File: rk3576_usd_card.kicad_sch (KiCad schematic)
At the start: 2 parts, among them U27 RK3576

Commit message: Add files via upload
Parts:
- renumbered C265 to C143, U27 to U2
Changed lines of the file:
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@@
 		(dnp no)
 		(fields_autoplaced yes)
-		(property "Reference" "C265"
+		(property "Reference" "C143"
 			(at 58.42 71.1262 0)
 			(show_name no)
@@
 		)
 		(property "Description" "Unpolarized capacitor, small symbol"
+			(at 60.96 72.39 0)
+			(hide yes)
+			(show_name no)
+			(do_not_autoplace no)
+			(effects
+				(font
+					(size 1.27 1.27)
+				)
+			)
+		)
+		(property "Dielectric" ""
+			(at 60.96 72.39 0)
+			(hide yes)
+			(show_name no)
+			(do_not_autoplace no)
+			(effects
+				(font
+					(size 1.27 1.27)
+				)
+			)
+		)
+		(property "Voltage" ""
+			(at 60.96 72.39 0)
+			(hide yes)
+			(show_name no)
+			(do_not_autoplace no)
+			(effects
+				(font
+					(size 1.27 1.27)
+				)
+			)
+		)
+		(property "KLC_S3.3" ""
+			(at 60.96 72.39 0)
+			(hide yes)
+			(show_name no)
+			(do_not_autoplace no)
+			(effects
+				(font
+					(size 1.27 1.27)
+				)
+			)
+		)
+		(property "KLC_S4.1" ""
+			(at 60.96 72.39 0)
+			(hide yes)
+			(show_name no)
+			(do_not_autoplace no)
+			(effects
+				(font
+					(size 1.27 1.27)
+				)
+			)
+		)
+		(property "KLC_S5.1" ""
 			(at 60.96 72.39 0)
 			(hide yes)
@@
 			(project "RK3576 SBC"
 				(path "/b79dbff4-0cad-4ff7-bec2-7c0e4f8b14d3/34f9b0cb-aeae-42b4-a2af-a0a79afcf392/e3169b31-7633-42aa-8b59-c93f8fc73ecf"
-					(reference "C265")
+					(reference "C143")
 					(unit 1)
 				)
@@
 		(in_pos_files yes)
 		(dnp no)
-		(property "Reference" "#PWR0352"
+		(property "Reference" "#PWR0205"
 			(at 60.96 81.28 0)
 			(hide yes)
@@
 			(project "RK3576 SBC"
 				(path "/b79dbff4-0cad-4ff7-bec2-7c0e4f8b14d3/34f9b0cb-aeae-42b4-a2af-a0a79afcf392/e3169b31-7633-42aa-8b59-c93f8fc73ecf"
-					(reference "#PWR0352")
+					(reference "#PWR0205")
 					(unit 1)
 				)
@@
 		(in_pos_files yes)
 		(dnp no)
-		(property "Reference" "#PWR0351"
+		(property "Reference" "#PWR0204"
 			(at 60.96 68.58 0)
 			(hide yes)
@@
 			(project "RK3576 SBC"
 				(path "/b79dbff4-0cad-4ff7-bec2-7c0e4f8b14d3/34f9b0cb-aeae-42b4-a2af-a0a79afcf392/e3169b31-7633-42aa-8b59-c93f8fc73ecf"
-					(reference "#PWR0351")
+					(reference "#PWR0204")
 					(unit 1)
 				)
@@
 		(dnp no)
 		(fields_autoplaced yes)
-		(property "Reference" "U27"
+		(property "Reference" "U2"
 			(at 101.6 62.23 0)
 			(show_name no)
@@
 		(property "Package" "FCCSP698L"
 			(at 101.6 72.39 0)
+			(show_name no)
+			(do_not_autoplace no)
+			(effects
+				(font
+					(size 1.27 1.27)
+				)
+			)
+		)
+		(property "Dielectric" ""
+			(at 101.6 87.63 0)
+			(hide yes)
+			(show_name no)
+			(do_not_autoplace no)
+			(effects
+				(font
+					(size 1.27 1.27)
+				)
+			)
+		)
+		(property "Voltage" ""
+			(at 101.6 87.63 0)
+			(hide yes)
+			(show_name no)
+			(do_not_autoplace no)
+			(effects
+				(font
+					(size 1.27 1.27)
+				)
+			)
+		)
+		(property "KLC_S3.3" ""
+			(at 101.6 87.63 0)
+			(hide yes)
+			(show_name no)
+			(do_not_autoplace no)
+			(effects
+				(font
+					(size 1.27 1.27)
+				)
+			)
+		)
+		(property "KLC_S4.1" ""
+			(at 101.6 87.63 0)
+			(hide yes)
+			(show_name no)
+			(do_not_autoplace no)
+			(effects
+				(font
+					(size 1.27 1.27)
+				)
+			)
+		)
+		(property "KLC_S5.1" ""
+			(at 101.6 87.63 0)
+			(hide yes)
 			(show_name no)
 			(do_not_autoplace no)
@@
 			(project "RK3576 SBC"
 				(path "/b79dbff4-0cad-4ff7-bec2-7c0e4f8b14d3/34f9b0cb-aeae-42b4-a2af-a0a79afcf392/e3169b31-7633-42aa-8b59-c93f8fc73ecf"
-					(reference "U27")
+					(reference "U2")
 					(unit 16)
 				)

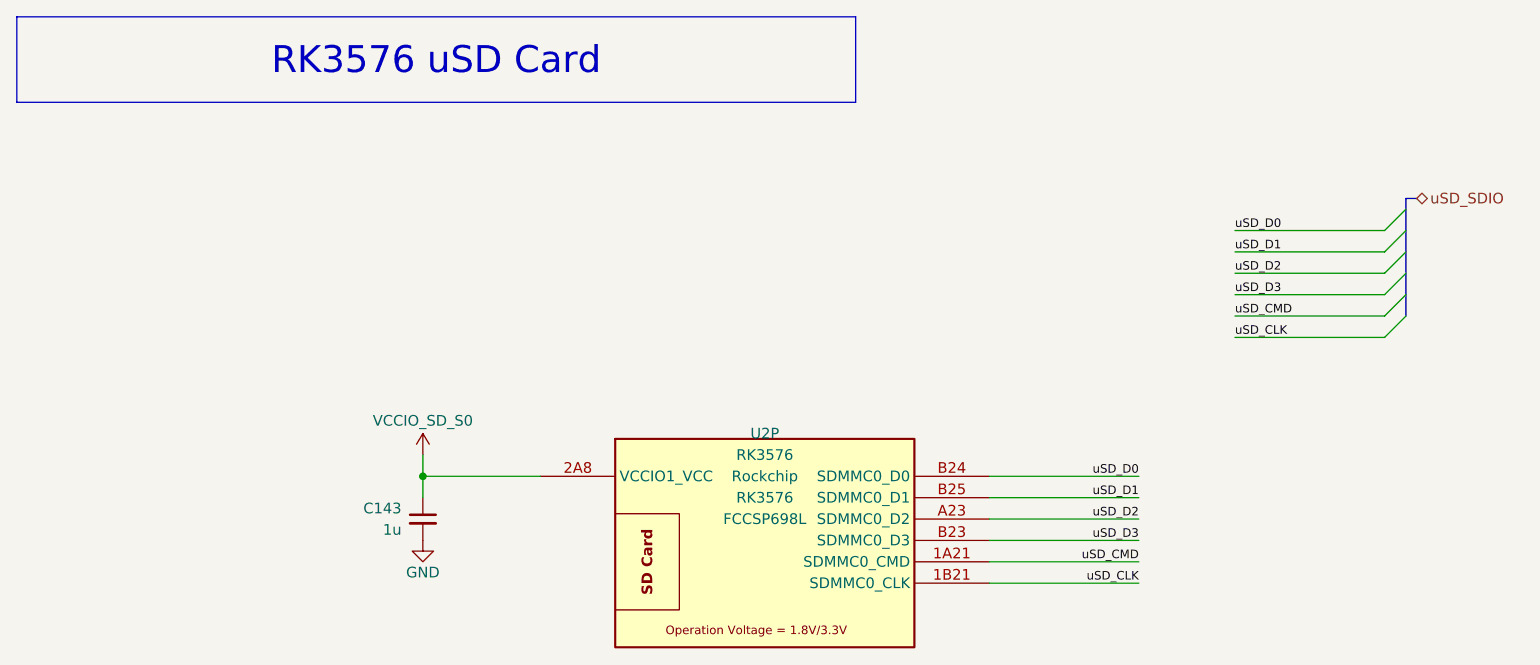
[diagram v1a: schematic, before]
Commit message: SBC Board V0.2
The SBC schematics before footprint and part number check
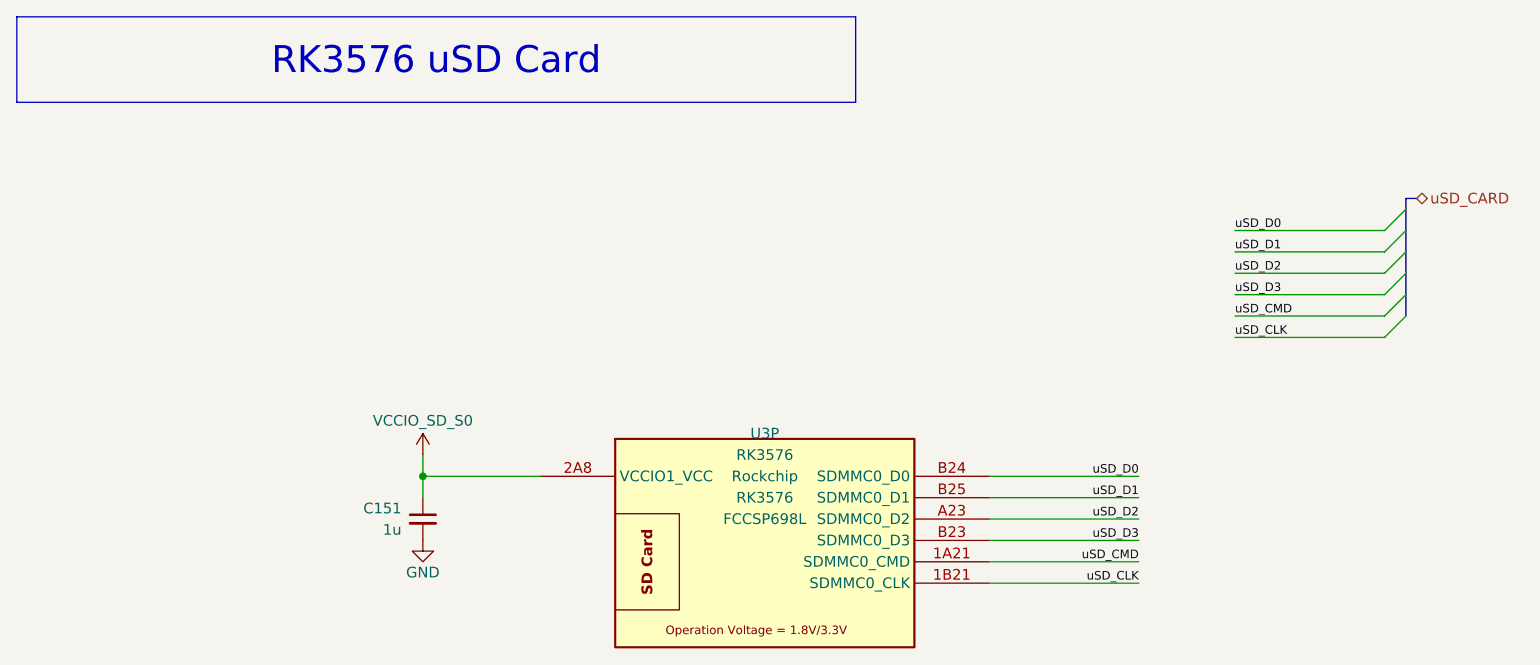
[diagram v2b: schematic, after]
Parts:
- U3: renamed from U2; footprint (none) -> easyeda2kicad:FCCSP-698_L17.2-W16.1-TL_RK3576
- renumbered C143 to C151
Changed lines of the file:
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@@
 		)
 	)
-	(hierarchical_label "uSD_SDIO"
+	(hierarchical_label "uSD_CARD"
 		(shape bidirectional)
 		(at 179.07 34.29 0)
+		(fields_autoplaced yes)
 		(effects
 			(font
@@
 			)
 			(justify left)
+		)
+		(property "Netclass" "uSD_CARD"
+			(at 179.07 35.56 0)
+			(hide yes)
+			(show_name no)
+			(do_not_autoplace no)
+			(effects
+				(font
+					(size 1.27 1.27)
+					(italic yes)
+				)
+				(justify left)
+			)
 		)
 	)
@@
 		(dnp no)
 		(fields_autoplaced yes)
-		(property "Reference" "C143"
+		(property "Reference" "C151"
 			(at 58.42 71.1262 0)
 			(show_name no)
@@
 			(project "RK3576 SBC"
 				(path "/b79dbff4-0cad-4ff7-bec2-7c0e4f8b14d3/34f9b0cb-aeae-42b4-a2af-a0a79afcf392/e3169b31-7633-42aa-8b59-c93f8fc73ecf"
-					(reference "C143")
+					(reference "C151")
 					(unit 1)
 				)
@@
 		(in_pos_files yes)
 		(dnp no)
-		(property "Reference" "#PWR0205"
+		(property "Reference" "#PWR0217"
 			(at 60.96 81.28 0)
 			(hide yes)
@@
 			(project "RK3576 SBC"
 				(path "/b79dbff4-0cad-4ff7-bec2-7c0e4f8b14d3/34f9b0cb-aeae-42b4-a2af-a0a79afcf392/e3169b31-7633-42aa-8b59-c93f8fc73ecf"
-					(reference "#PWR0205")
+					(reference "#PWR0217")
 					(unit 1)
 				)
@@
 		(in_pos_files yes)
 		(dnp no)
-		(property "Reference" "#PWR0204"
+		(property "Reference" "#PWR0216"
 			(at 60.96 68.58 0)
 			(hide yes)
@@
 			(project "RK3576 SBC"
 				(path "/b79dbff4-0cad-4ff7-bec2-7c0e4f8b14d3/34f9b0cb-aeae-42b4-a2af-a0a79afcf392/e3169b31-7633-42aa-8b59-c93f8fc73ecf"
-					(reference "#PWR0204")
+					(reference "#PWR0216")
 					(unit 1)
 				)
@@
 		(dnp no)
 		(fields_autoplaced yes)
-		(property "Reference" "U2"
+		(property "Reference" "U3"
 			(at 101.6 62.23 0)
 			(show_name no)
@@
 			)
 		)
-		(property "Footprint" ""
+		(property "Footprint" "easyeda2kicad:FCCSP-698_L17.2-W16.1-TL_RK3576"
 			(at 34.29 24.765 0)
 			(hide yes)
@@
 			(project "RK3576 SBC"
 				(path "/b79dbff4-0cad-4ff7-bec2-7c0e4f8b14d3/34f9b0cb-aeae-42b4-a2af-a0a79afcf392/e3169b31-7633-42aa-8b59-c93f8fc73ecf"
-					(reference "U2")
+					(reference "U3")
 					(unit 16)
 				)

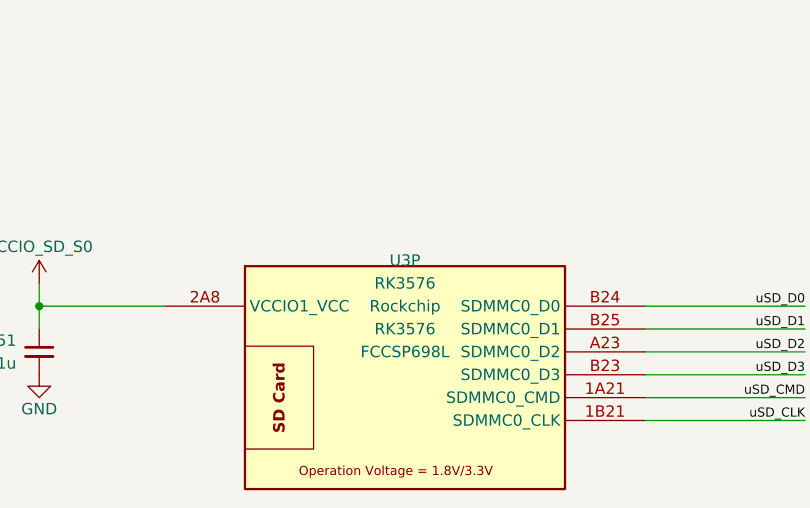
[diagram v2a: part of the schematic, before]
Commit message: SBCv0.3
there is no big thing update just some LCSC & Mouser parts
and Big problem deleted alot of component values (:
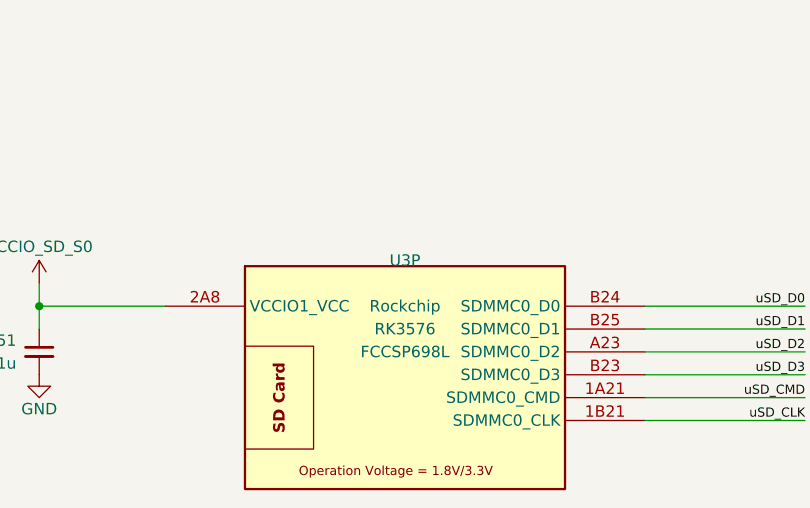
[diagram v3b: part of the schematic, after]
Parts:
- C151: footprint Capacitor_SMD:C_0402_1005Metric_Pad0.74x0.62mm_HandSolder -> Capacitor_SMD:C_0201_0603Metric_Pad0.64x0.40mm_HandSolder; LCSC Part (none) -> C5209398; Mouser Part (none) -> CL03A105KP3NSNC
- U3: value RK3576 -> (none); LCSC Part (none) -> (polyline
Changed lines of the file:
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@@
 			)
 		)
-		(property "Footprint" "Capacitor_SMD:C_0402_1005Metric_Pad0.74x0.62mm_HandSolder"
+		(property "Footprint" "Capacitor_SMD:C_0201_0603Metric_Pad0.64x0.40mm_HandSolder"
 			(at 60.96 72.39 0)
 			(hide yes)
@@
 			)
 		)
-		(property "KLC_S5.1" ""
+		(property "LCSC Part" "C5209398"
+			(at 60.96 72.39 0)
+			(hide yes)
+			(show_name no)
+			(do_not_autoplace no)
+			(effects
+				(font
+					(size 1.27 1.27)
+				)
+			)
+		)
+		(property "Mouser Part" "CL03A105KP3NSNC "
+			(at 60.96 72.39 0)
+			(hide yes)
+			(show_name no)
+			(do_not_autoplace no)
+			(effects
+				(font
+					(size 1.27 1.27)
+				)
+			)
+		)
+		(property "KLC_S4.2_DVDD" ""
+			(at 60.96 72.39 0)
+			(hide yes)
+			(show_name no)
+			(do_not_autoplace no)
+			(effects
+				(font
+					(size 1.27 1.27)
+				)
+			)
+		)
+		(property "KLC_S4.2_VREG_LX" ""
 			(at 60.96 72.39 0)
 			(hide yes)
@@
 					(reference "C151")
 					(unit 1)
+					(variant
+						(name "Test")
+					)
 				)
 			)
@@
 			)
 		)
-		(property "Value" "RK3576"
+		(property "Value" ""
 			(at 101.6 64.77 0)
 			(show_name no)
@@
 			)
 		)
-		(property "KLC_S5.1" ""
+		(property "LCSC Part" "(polyline"
+			(at 101.6 87.63 0)
+			(hide yes)
+			(show_name no)
+			(do_not_autoplace no)
+			(effects
+				(font
+					(size 1.27 1.27)
+				)
+			)
+		)
+		(property "KLC_S4.2_DVDD" ""
+			(at 101.6 87.63 0)
+			(hide yes)
+			(show_name no)
+			(do_not_autoplace no)
+			(effects
+				(font
+					(size 1.27 1.27)
+				)
+			)
+		)
+		(property "KLC_S4.2_VREG_LX" ""
 			(at 101.6 87.63 0)
 			(hide yes)
@@
 					(reference "U3")
 					(unit 16)
-				)
-			)
+					(variant
+						(name "Test")
+					)
+				)
+			)

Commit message: SBCv0.4
add LCSC & Mouser parts 
and solve the deleted value in the past version
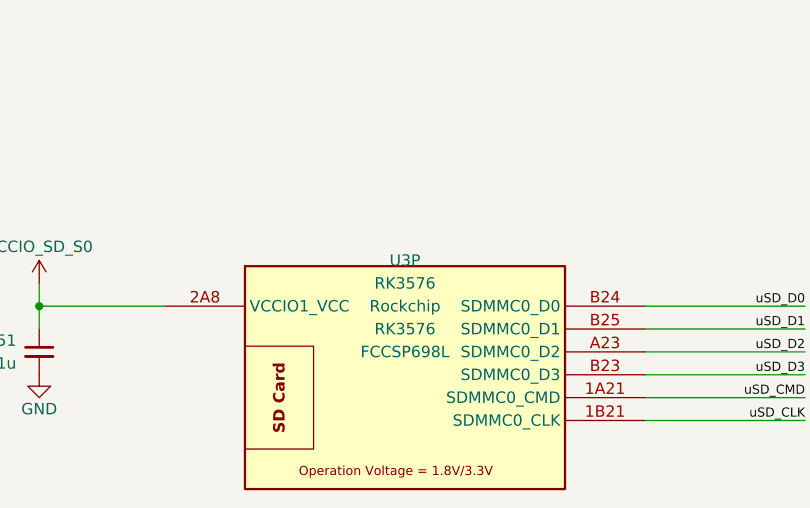
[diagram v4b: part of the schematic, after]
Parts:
- U3: value (none) -> RK3576; LCSC Part (polyline -> C42388007
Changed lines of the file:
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@@
 			)
 		)
-		(property "Value" ""
+		(property "Value" "RK3576"
 			(at 101.6 64.77 0)
 			(show_name no)
@@
 			)
 		)
-		(property "LCSC Part" "(polyline"
+		(property "LCSC Part" "C42388007"
 			(at 101.6 87.63 0)
 			(hide yes)
